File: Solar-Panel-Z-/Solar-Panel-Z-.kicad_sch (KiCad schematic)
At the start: 65 parts, among them J1 FFC2B28-10-G, J2 U.FL-R-SMT-1, Q1 IRLML2803, U1 Value, U2 TSL2561, U3 NDS8434, U4 ATB2012-50011-T000

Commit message: Exported Gerbers
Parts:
- added H3, H4, H5, H6: MountingHole, MountingHole:MountingHole_2.2mm_M2_DIN965, symbol Mechanical:MountingHole
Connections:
- net GND: no longer U4.5 (GND), U4.6 (GND)
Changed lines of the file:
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@@
     (pin "8")
+  )
+  (symbol (lib_id "Mechanical:MountingHole") (at 22.225 141.986 0) (unit 1)
+    (in_bom yes) (on_board yes) (fields_autoplaced)
+    (property "Reference" "H6" (id 0) (at 24.765 141.1513 0)
+      (effects (font (size 1.27 1.27)) (justify left))
+    )
+    (property "Value" "MountingHole" (id 1) (at 24.765 143.6882 0)
+      (effects (font (size 1.27 1.27)) (justify left))
+    )
+    (property "Footprint" "MountingHole:MountingHole_2.2mm_M2_DIN965" (id 2) (at 22.225 141.986 0)
+      (effects (font (size 1.27 1.27)) hide)
+    )
+    (property "Datasheet" "~" (id 3) (at 22.225 141.986 0)
+      (effects (font (size 1.27 1.27)) hide)
+    )
   )
   (symbol (lib_id "Device:C") (at 176.276 74.676 0) (unit 1)
@@
     (pin "3")
     (pin "4")
-    (pin "5")
-    (pin "6")
+  )
+  (symbol (lib_id "Mechanical:MountingHole") (at 22.098 135.636 0) (unit 1)
+    (in_bom yes) (on_board yes) (fields_autoplaced)
+    (property "Reference" "H5" (id 0) (at 24.638 134.8013 0)
+      (effects (font (size 1.27 1.27)) (justify left))
+    )
+    (property "Value" "MountingHole" (id 1) (at 24.638 137.3382 0)
+      (effects (font (size 1.27 1.27)) (justify left))
+    )
+    (property "Footprint" "MountingHole:MountingHole_2.2mm_M2_DIN965" (id 2) (at 22.098 135.636 0)
+      (effects (font (size 1.27 1.27)) hide)
+    )
+    (property "Datasheet" "~" (id 3) (at 22.098 135.636 0)
+      (effects (font (size 1.27 1.27)) hide)
+    )
   )
   (symbol (lib_id "Device:C") (at 195.58 34.29 0) (unit 1)
@@
     (pin "1")
     (pin "2")
+  )
+  (symbol (lib_id "Mechanical:MountingHole") (at 22.098 123.19 0) (unit 1)
+    (in_bom yes) (on_board yes) (fields_autoplaced)
+    (property "Reference" "H3" (id 0) (at 24.638 122.3553 0)
+      (effects (font (size 1.27 1.27)) (justify left))
+    )
+    (property "Value" "MountingHole" (id 1) (at 24.638 124.8922 0)
+      (effects (font (size 1.27 1.27)) (justify left))
+    )
+    (property "Footprint" "MountingHole:MountingHole_2.2mm_M2_DIN965" (id 2) (at 22.098 123.19 0)
+      (effects (font (size 1.27 1.27)) hide)
+    )
+    (property "Datasheet" "~" (id 3) (at 22.098 123.19 0)
+      (effects (font (size 1.27 1.27)) hide)
+    )
   )
   (symbol (lib_id "Device:C") (at 23.876 182.372 180) (unit 1)
@@
     (pin "1")
     (pin "2")
+  )
+  (symbol (lib_id "Mechanical:MountingHole") (at 22.098 129.413 0) (unit 1)
+    (in_bom yes) (on_board yes) (fields_autoplaced)
+    (property "Reference" "H4" (id 0) (at 24.638 128.5783 0)
+      (effects (font (size 1.27 1.27)) (justify left))
+    )
+    (property "Value" "MountingHole" (id 1) (at 24.638 131.1152 0)
+      (effects (font (size 1.27 1.27)) (justify left))
+    )
+    (property "Footprint" "MountingHole:MountingHole_2.2mm_M2_DIN965" (id 2) (at 22.098 129.413 0)
+      (effects (font (size 1.27 1.27)) hide)
+    )
+    (property "Datasheet" "~" (id 3) (at 22.098 129.413 0)
+      (effects (font (size 1.27 1.27)) hide)
+    )
   )
   (symbol (lib_id "solarpanels:U.FL-R-SMT-1") (at 109.474 176.53 0) (mirror y) (unit 1)
@@
       (reference "H2") (unit 1) (value "MountingHole_Pad") (footprint "solarpanels:Antenna Pad")
     )
+    (path "/b9a867ad-70c3-403b-8dbc-e360f8d87bd9"
+      (reference "H3") (unit 1) (value "MountingHole") (footprint "MountingHole:MountingHole_2.2mm_M2_DIN965")
+    )
+    (path "/e88d01b1-e5ca-4741-addf-c39e2d0bfbd5"
+      (reference "H4") (unit 1) (value "MountingHole") (footprint "MountingHole:MountingHole_2.2mm_M2_DIN965")
+    )
+    (path "/770e1af7-abe4-4f50-9e07-aaeeeeda7425"
+      (reference "H5") (unit 1) (value "MountingHole") (footprint "MountingHole:MountingHole_2.2mm_M2_DIN965")
+    )
+    (path "/137a7213-3484-4517-87fb-445aeea88cde"
+      (reference "H6") (unit 1) (value "MountingHole") (footprint "MountingHole:MountingHole_2.2mm_M2_DIN965")
+    )
     (path "/dcfad885-589c-40f1-b2d4-7abf101b9dad"

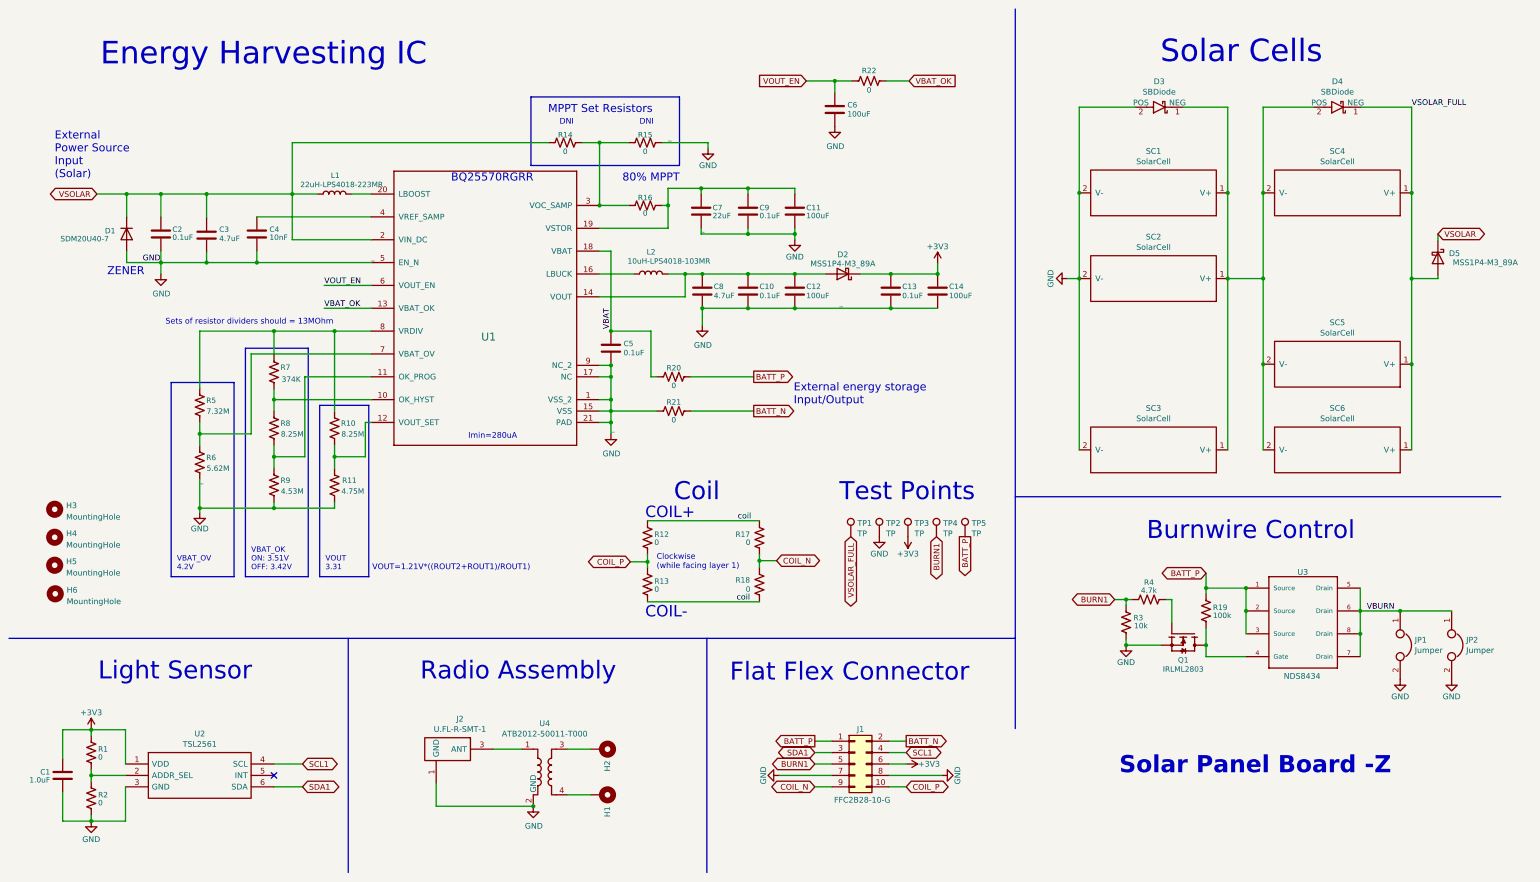
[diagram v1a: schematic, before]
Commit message: Stack architecture schematic updates / fixes
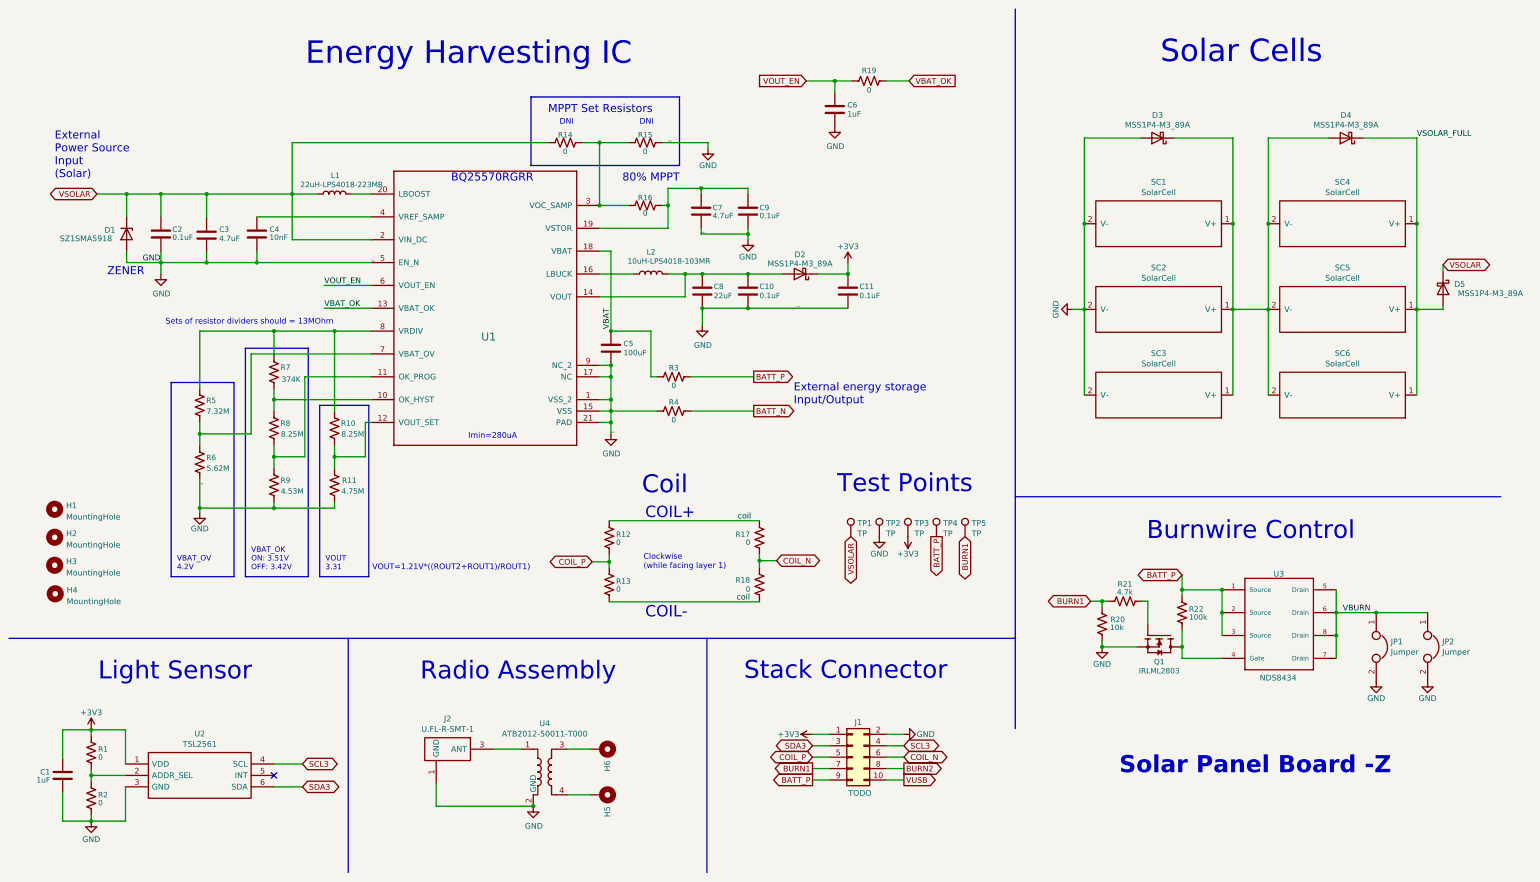
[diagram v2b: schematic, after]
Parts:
- removed C11, C12, C14: 100uF, Capacitor_SMD:C_0603_1608Metric, symbol Device:C
- removed D1: SDM20U40-7, Diode_SMD:D_SOD-523, symbol Device:D
- removed D3, D4: SBDiode, solarpanels:SB Diode, symbol solarpanels:SBDiode
- added D1: SZ1SMA5918, Diode_SMD:D_SMA, symbol Diode:Z1SMAxxx
- added D3, D4: MSS1P4-M3_89A, solarpanels:MICROSMP, symbol Device:D_Schottky
- C1: value 1.0uF -> 1uF; footprint Capacitor_SMD:C_0402_1005Metric -> Capacitor_SMD:C_0603_1608Metric
- C10, C2, C3, C4, C9: footprint Capacitor_SMD:C_0402_1005Metric -> Capacitor_SMD:C_0603_1608Metric
- C11: renamed from C13; footprint Capacitor_SMD:C_0402_1005Metric -> Capacitor_SMD:C_0603_1608Metric
- C5: value 0.1uF -> 100uF; footprint Capacitor_SMD:C_0402_1005Metric -> Capacitor_SMD:C_0805_2012Metric
- C6: value 100uF -> 1uF
- C7: value 22uF -> 4.7uF; footprint Capacitor_SMD:C_0402_1005Metric -> Capacitor_SMD:C_0603_1608Metric
- C8: value 4.7uF -> 22uF; footprint Capacitor_SMD:C_0402_1005Metric -> Capacitor_SMD:C_0603_1608Metric
- J1: value FFC2B28-10-G -> TODO
- R1, R10, R11, R12, R13, R14, R15, R16, R17, R18, R2, R5, R6, R7, R8, R9: footprint Resistor_SMD:R_0402_1005Metric -> Resistor_SMD:R_0603_1608Metric
- R19: renamed from R22; footprint Resistor_SMD:R_0402_1005Metric -> Resistor_SMD:R_0603_1608Metric
- R20: renamed from R3; footprint Resistor_SMD:R_0402_1005Metric -> Resistor_SMD:R_0603_1608Metric
- R21: renamed from R4; footprint Resistor_SMD:R_0402_1005Metric -> Resistor_SMD:R_0603_1608Metric
- R22: renamed from R19; footprint Resistor_SMD:R_0402_1005Metric -> Resistor_SMD:R_0603_1608Metric
- R3: renamed from R20; footprint Resistor_SMD:R_0402_1005Metric -> Resistor_SMD:R_0603_1608Metric
- R4: renamed from R21; footprint Resistor_SMD:R_0402_1005Metric -> Resistor_SMD:R_0603_1608Metric
- U1: value Value -> BQ25570RGRR
- renumbered H3 to H1, H4 to H2, H5 to H3, H6 to H4, H1 to H5, H2 to H6
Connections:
- net +3V3: now also J1.1 (Pin_1); no longer J1.6 (Pin_6)
- net BATT_N: no longer J1.2 (Pin_2)
- net BATT_P: now also J1.9 (Pin_9), TP4.1; no longer J1.1 (Pin_1), TP5.1
- net BURN1: now also J1.7 (Pin_7), TP5.1; no longer J1.5 (Pin_5), TP4.1
- net COIL_N: now also J1.6 (Pin_6); no longer J1.9 (Pin_9)
- net COIL_P: now also J1.5 (Pin_5); no longer J1.10 (Pin_10)
- net GND: now also J1.2 (Pin_2), D1.2 (A), D3.2 (A); no longer J1.7 (Pin_7), J1.8 (Pin_8)
- net VSOLAR: now also TP1.1, D1.1 (K)
- net VSOLAR_FULL: now also D4.1 (K); no longer TP1.1
- net at SC1.1 (V+), SC2.1 (V+), SC3.1 (V+)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: now also D3.1 (K), D4.2 (A)
- net SCL1 renamed SCL3
- net SDA1 renamed SDA3
- new net BURN2: J1.8 (Pin_8)
- new net VUSB: J1.10 (Pin_10)
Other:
- note added: "Stack Connector"
- note removed: "Flat Flex Connector"
- moved on the sheet: C11, D2, D5, JP1, JP2, Q1, R12, R13, R20, R21, R22, SC1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

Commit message: Correct positions for everything except coils
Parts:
- J1: footprint solarpanels:GCT_FFC2B28-10-G -> batteryboard:FTS-105-XX-YY-DV-A
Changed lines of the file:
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@@
     (property "Reference" "J1" (id 0) (at 200.787 170.561 0))
     (property "Value" "TODO" (id 1) (at 201.168 186.309 0))
-    (property "Footprint" "solarpanels:GCT_FFC2B28-10-G" (id 2) (at 199.517 178.308 0)
+    (property "Footprint" "batteryboard:FTS-105-XX-YY-DV-A" (id 2) (at 199.517 178.308 0)
       (effects (font (size 1.27 1.27)) hide)
     )
@@
     )
     (path "/7b56f989-5970-46f1-b459-f3376f77fccc"
-      (reference "J1") (unit 1) (value "TODO") (footprint "solarpanels:GCT_FFC2B28-10-G")
+      (reference "J1") (unit 1) (value "TODO") (footprint "batteryboard:FTS-105-XX-YY-DV-A")
     )
     (path "/ea2e338d-b9c8-4965-a217-a9a6c3864d0c"

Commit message: Finish 6 Layer panel versions
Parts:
- removed H1, H2, H3, H4: MountingHole, MountingHole:MountingHole_2.2mm_M2_DIN965, symbol Mechanical:MountingHole
- removed Q1: IRLML2803, Package_TO_SOT_SMD:SOT-23, symbol solarpanels:IRLML2803TRPBF
- removed SC5, SC6: SolarCell, solarpanels:KXOB25-05X3F, symbol solarpanels:SolarCell_Small
- removed TP5: TP, TestPoint:TestPoint_THTPad_D1.0mm_Drill0.5mm, symbol Connector:TestPoint
- removed U3: NDS8434, solarpanels:NDS8434, symbol solarpanels:symbols_NDS8434
- removed U4: ATB2012-50011-T000, solarpanels:ATB2012, symbol solarpanels:ATB2012
- added C12, C13: 10nF, Capacitor_SMD:C_0603_1608Metric, symbol Device:C
- added H1, H2, H3, H4: MountingHole, MountingHole:MountingHole_2.2mm_M2_DIN965_Pad, symbol Mechanical:MountingHole_Pad
- added Q1, Q3: BSS138DWQ-7, Package_TO_SOT_SMD:SOT-363_SC-70-6, symbol mainboard:BSS138DWQ-7
- added Q2, Q4: MBT2222ADW1T1, Package_TO_SOT_SMD:SOT-363_SC-70-6, symbol Transistor_BJT:MBT2222ADW1T1
- added Q5: IRLML2803, Package_TO_SOT_SMD:SOT-23, symbol solarpanels:IRLML2803TRPBF
- added R23, R24, R28, R29, R31: 10K, Resistor_SMD:R_0603_1608Metric, symbol Device:R_US
- added R25, R30: 200K, Resistor_SMD:R_0603_1608Metric, symbol Device:R_US
- added R26: 680, Resistor_SMD:R_0603_1608Metric, symbol Device:R_US
- added R27, R33: 100K, Resistor_SMD:R_0603_1608Metric, symbol Device:R_US
- added R32: 4.7K, Resistor_SMD:R_0603_1608Metric, symbol Device:R_US
- added U3: ATB2012-50011-T000, solarpanels:ATB2012, symbol solarpanels:ATB2012
- added U4: NDS8434, solarpanels:NDS8434, symbol solarpanels:symbols_NDS8434
- C1: footprint Capacitor_SMD:C_0603_1608Metric -> Capacitor_SMD:C_0402_1005Metric
- D1: value SZ1SMA5918 -> SZMM5Z5V1T1G; footprint Diode_SMD:D_SMA -> Diode_SMD:D_SOD-523
- H5, H6: footprint solarpanels:Antenna Pad -> solarpanels:Antenna Mount
- J1: value TODO -> FTS-105-01-L-DV-A; footprint batteryboard:FTS-105-XX-YY-DV-A -> solarpanels:SAMTEC-FTS-105-01-X-DV-A
- JP1, JP2: footprint solarpanels:Burn-Wire-Rotated -> solarpanels:Burn-Wire
- R1, R2: footprint Resistor_SMD:R_0603_1608Metric -> Resistor_SMD:R_0402_1005Metric
- R14, R15: value 0 -> DNI
- R19: value 0 -> DNI; DNI (none) -> DNI
- R20: value 10k -> DNI; DNI (none) -> DNI
- R21: value 4.7k -> 680
- R22: value 100k -> 100K
- SC1, SC2, SC3, SC4: value SolarCell -> SolarCell_Small
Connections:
- net BATT_N is gone; now on net VBAT_OK: R4.1
- net VUSB is gone; now on net BATT_P: J1.10 (Pin_10)
- net +3V3: now also R22.1, R23.1, R24.1, R27.1, R28.1, R29.1
- net BATT_P: now also R33.2, U4.1 (Source), U4.2 (Source), U4.3 (Source); no longer R22.2, TP4.1
- net BURN1: now also J1.3 (Pin_3), R31.1, R32.2; no longer J1.7 (Pin_7), R20.1, R21.2
- net GND: now also J1.4 (Pin_4), C12.2, C13.2, H1.1, H2.1, H3.1, H4.1, Q1.1 (S2), Q1.4 (S1), Q3.1 (S2), Q3.4 (S1), Q5.2 (S), R31.2, U3.2 (GND); no longer R20.2, R4.2, SC3.2 (V-)
- net VBAT: now also TP4.1
- net VBAT_OK: no longer R19.1
- net VBURN: now also U4.5 (Drain), U4.6 (Drain), U4.7 (Drain), U4.8 (Drain)
- net VOUT_EN: now also R4.2; no longer R19.2
- net VSOLAR_FULL: now also SC3.1 (V+)
- net at D3.1 (K), D4.2 (A), SC1.1 (V+)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: now also SC3.2 (V-); no longer SC3.1 (V+)
- net at H5.1: now also U3.4
- net at R21.1: now also Q2.2 (B1)
- net at J2.3 (ANT): now also U3.1
- net at H6.1: now also U3.3
- net BURN2 renamed SCL
- net SCL: now also R19.2, Q2.1 (E1), Q2.3 (C2)
- net SCL3 renamed SCL_LS
- net SCL_LS: now also R19.1, Q2.4 (E2), Q2.6 (C1), R24.2, R25.1; no longer J1.4 (Pin_4)
- net SDA3 renamed SDA_LS
- net SDA_LS: now also R20.1, Q4.4 (E2), Q4.6 (C1), R29.2, R30.1; no longer J1.3 (Pin_3)
- new net: Q1.6 (D1), Q2.5 (B2), R21.2, R23.2
- new net: C12.1, Q1.5 (G1), R25.2
- new net: Q3.2 (G2), Q3.3 (D2), R27.2
- new net: Q3.6 (D1), Q4.5 (B2), R26.2, R28.2
- new net: Q1.2 (G2), Q1.3 (D2), R22.2
- new net: Q5.1 (G), R32.1
- new net: C13.1, Q3.5 (G1), R30.2
- new net: Q4.2 (B1), R26.1
- new net: Q5.3 (D), R33.1, U4.4 (Gate)
- new net SDA: J1.7 (Pin_7), Q4.1 (E1), Q4.3 (C2), R20.2
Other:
- note added: "->"
- note added: "<-"
- note added: "Arrows indicate clockwise (while facing layer 1)"
- note added: "I2C Bus Protection - Light Sensor"
- note added: "Only one resistor per side (COIL_P/COIL_N) should be populated. R12 and R18 should nominally be correct."
- note added: "Solar Panel Board Z-"
- note removed: "Burnwire Control"
- note removed: "Clockwise (while facing layer 1)"
- note removed: "Radio Assembly"
- note removed: "Solar Panel Board -Z"
